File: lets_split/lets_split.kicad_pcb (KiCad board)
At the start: 2 copper layers, 112 x 79 mm, 62 parts, among them J1 3PIN, J2 6PIN, J3 3PIN, SW1 SW_PUSH, SW10 SW_PUSH, SW11 SW_PUSH, SW12 SW_PUSH, SW13 SW_PUSH, SW14 SW_PUSH, SW15 SW_PUSH, SW16 SW_PUSH, SW17 SW_PUSH, SW18 SW_PUSH, SW19 SW_PUSH, SW2 SW_PUSH, SW21 SW_PUSH, SW22 SW_PUSH, SW23 SW_PUSH, SW3 SW_PUSH, SW4 SW_PUSH, SW5 SW_PUSH, SW6 SW_PUSH, SW7 SW_PUSH, SW8 SW_PUSH, SW9 SW_PUSH, U2 HOLE, U3 HOLE, U4 HOLE, U5 HOLE

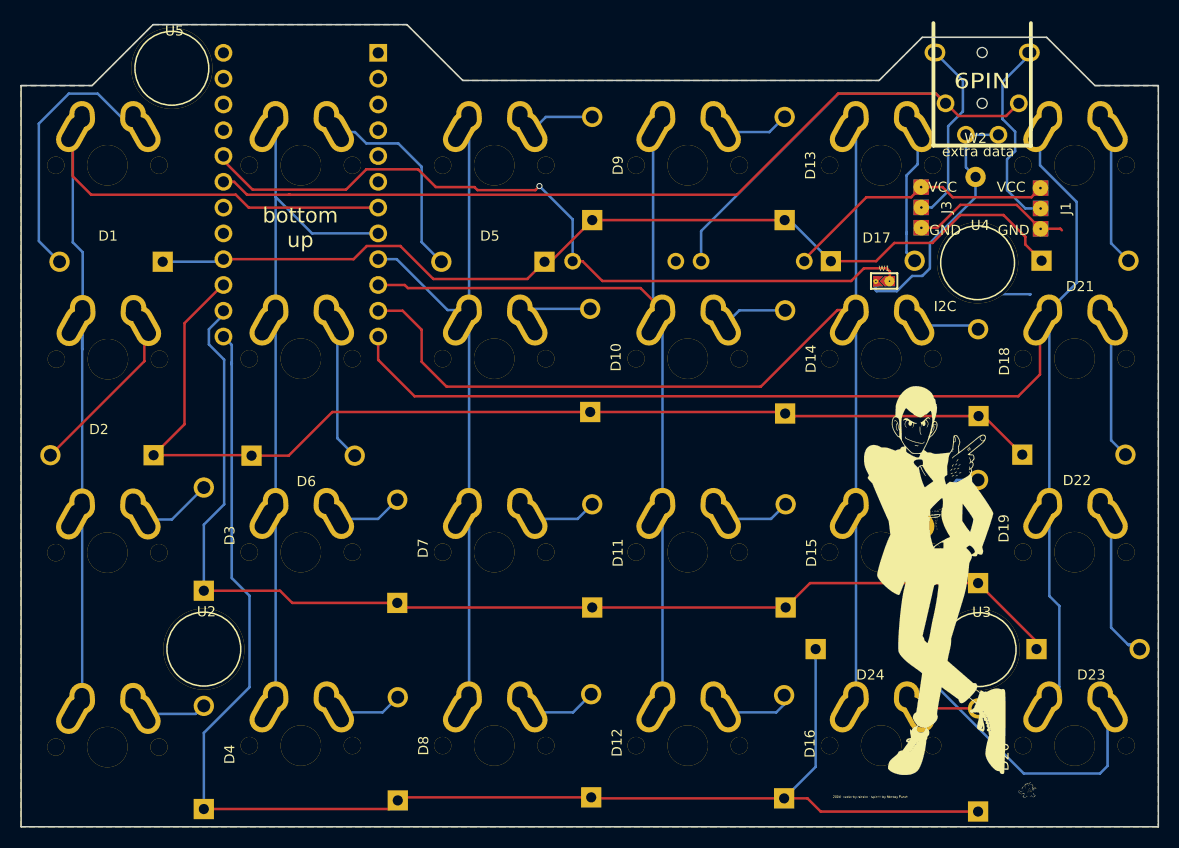
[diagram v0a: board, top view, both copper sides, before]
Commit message: Fix column 1 spacing
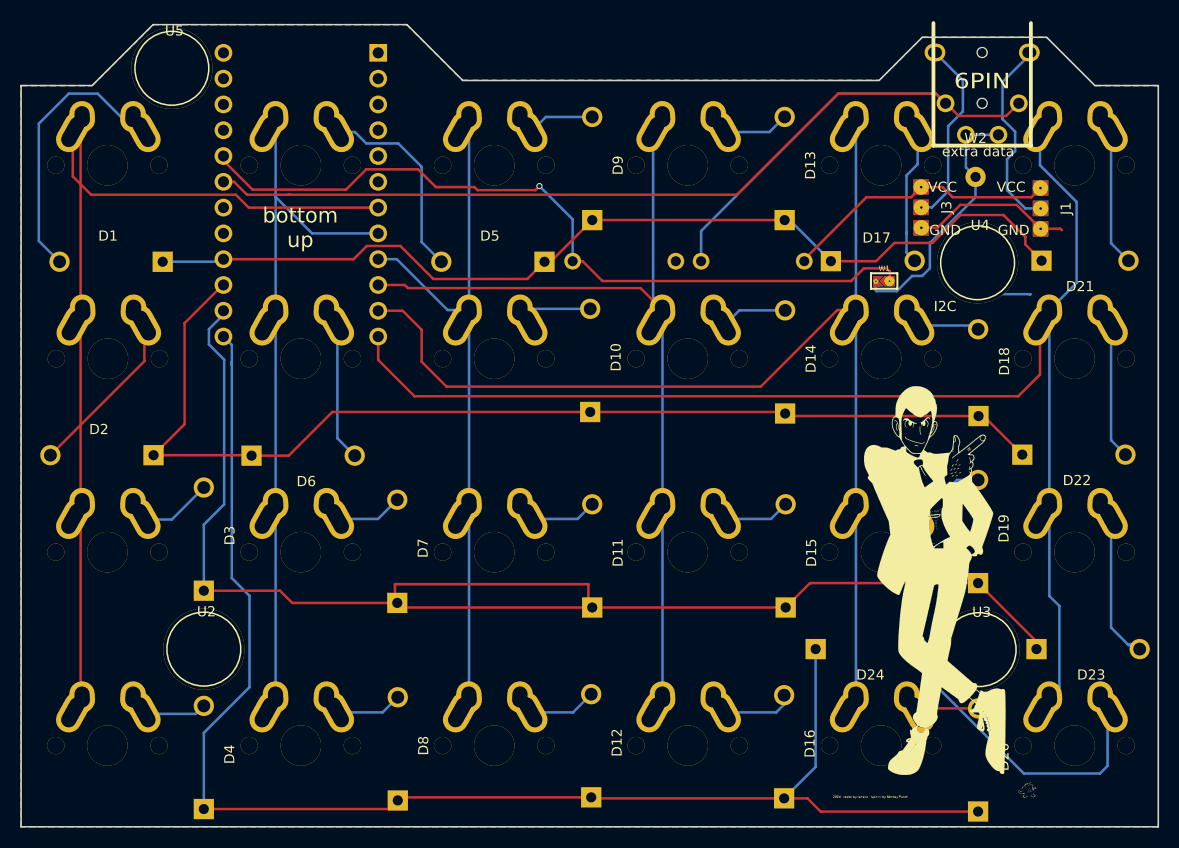
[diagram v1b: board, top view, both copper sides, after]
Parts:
- moved SW4 0.15 mm to (45.5, 104.0)
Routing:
- net row2: track 117.3 -> 142.1 mm
- net col0: track 96.5 -> 98.4 mm
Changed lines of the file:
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@@
-(kicad_pcb (version 4) (host pcbnew 4.0.2-stable)
+(kicad_pcb (version 4) (host pcbnew 4.0.7)
   (general
     (links 160)
-    (no_connects 2)
-    (area 36.386172 31.485 149.075001 114.5692)
+    (no_connects 0)
+    (area 35.71875 30.95625 150.01875 114.3)
     (thickness 1.6)
     (drawings 29)
-    (tracks 287)
+    (tracks 291)
     (zones 0)
     (modules 62)
@@
     (add_net xtradata)
   )
+  (module flipalps:MXALPS_FLIP (layer F.Cu)
+    (at 45.55 65.9)
+    (descr MXALPS)
+    (tags MXALPS)
+    (fp_text reference SW2 (at 0 3.048) (layer B.SilkS) hide
+      (effects (font (thickness 0.3048)) (justify mirror))
+    )
+    (fp_text value SW_PUSH (at -3.5 9) (layer B.SilkS) hide
+      (effects (font (thickness 0.3048)) (justify mirror))
+    )
+    (fp_line (start -7.75 6.4) (end -7.75 -6.4) (layer Dwgs.User) (width 0.3))
+    (fp_line (start -7.75 6.4) (end 7.75 6.4) (layer Dwgs.User) (width 0.3))
+    (fp_line (start 7.75 6.4) (end 7.75 -6.4) (layer Dwgs.User) (width 0.3))
+    (fp_line (start 7.75 -6.4) (end -7.75 -6.4) (layer Dwgs.User) (width 0.3))
+    (fp_line (start -7.62 -7.62) (end 7.62 -7.62) (layer Dwgs.User) (width 0.3))
+    (fp_line (start 7.62 -7.62) (end 7.62 7.62) (layer Dwgs.User) (width 0.3))
+    (fp_line (start 7.62 7.62) (end -7.62 7.62) (layer Dwgs.User) (width 0.3))
+    (fp_line (start -7.62 7.62) (end -7.62 -7.62) (layer Dwgs.User) (width 0.3))
+    (pad 1 thru_hole oval (at -2.48 -4.79 3.9) (size 2.5 3.08) (drill oval 1.5 2.08) (layers *.Cu *.Mask F.SilkS)
+      (net 36 col0))
+    (pad 2 thru_hole oval (at 3.595 -3.27 29) (size 2.5 4.17) (drill oval 1.5 3.17) (layers *.Cu *.Mask F.SilkS)
+      (net 3 "Net-(D2-Pad2)"))
+    (pad "" np_thru_hole circle (at 0 0) (size 3.98781 3.98781) (drill 3.9878) (layers *.Cu *.Mask F.SilkS)
+      (clearance 0.1524))
+    (pad "" np_thru_hole circle (at -5.08 0) (size 1.70181 1.70181) (drill 1.7018) (layers *.Cu *.Mask F.SilkS)
+      (clearance 0.1524))
+    (pad "" np_thru_hole circle (at 5.08 0) (size 1.70181 1.70181) (drill 1.7018) (layers *.Cu *.Mask F.SilkS)
+      (clearance 0.1524))
+    (pad 1 thru_hole oval (at -3.405 -3.27 330.95) (size 2.5 4.17) (drill oval 1.5 3.17) (layers *.Cu *.Mask F.SilkS)
+      (net 36 col0))
+    (pad 2 thru_hole oval (at 2.52 -4.79 356.1) (size 2.5 3.08) (drill oval 1.5 2.08) (layers *.Cu *.Mask F.SilkS)
+      (net 3 "Net-(D2-Pad2)"))
+  )
   (module Diodes_ThroughHole:Diode_DO-41_SOD81_Horizontal_RM10 (layer F.Cu)
     (at 131.25 110.5 90)
@@
   )
   (module flipalps:MXALPS_FLIP (layer F.Cu)
-    (at 45.55 65.95)
-    (descr MXALPS)
-    (tags MXALPS)
-    (fp_text reference SW2 (at 0 3.048) (layer B.SilkS) hide
-      (effects (font (thickness 0.3048)) (justify mirror))
-    )
-    (fp_text value SW_PUSH (at -3.5 9) (layer B.SilkS) hide
-      (effects (font (thickness 0.3048)) (justify mirror))
-    )
-    (fp_line (start -7.75 6.4) (end -7.75 -6.4) (layer Dwgs.User) (width 0.3))
-    (fp_line (start -7.75 6.4) (end 7.75 6.4) (layer Dwgs.User) (width 0.3))
-    (fp_line (start 7.75 6.4) (end 7.75 -6.4) (layer Dwgs.User) (width 0.3))
-    (fp_line (start 7.75 -6.4) (end -7.75 -6.4) (layer Dwgs.User) (width 0.3))
-    (fp_line (start -7.62 -7.62) (end 7.62 -7.62) (layer Dwgs.User) (width 0.3))
-    (fp_line (start 7.62 -7.62) (end 7.62 7.62) (layer Dwgs.User) (width 0.3))
-    (fp_line (start 7.62 7.62) (end -7.62 7.62) (layer Dwgs.User) (width 0.3))
-    (fp_line (start -7.62 7.62) (end -7.62 -7.62) (layer Dwgs.User) (width 0.3))
-    (pad 1 thru_hole oval (at -2.48 -4.79 3.9) (size 2.5 3.08) (drill oval 1.5 2.08) (layers *.Cu *.Mask F.SilkS)
-      (net 36 col0))
-    (pad 2 thru_hole oval (at 3.595 -3.27 29) (size 2.5 4.17) (drill oval 1.5 3.17) (layers *.Cu *.Mask F.SilkS)
-      (net 3 "Net-(D2-Pad2)"))
-    (pad "" np_thru_hole circle (at 0 0) (size 3.98781 3.98781) (drill 3.9878) (layers *.Cu *.Mask F.SilkS)
-      (clearance 0.1524))
-    (pad "" np_thru_hole circle (at -5.08 0) (size 1.70181 1.70181) (drill 1.7018) (layers *.Cu *.Mask F.SilkS)
-      (clearance 0.1524))
-    (pad "" np_thru_hole circle (at 5.08 0) (size 1.70181 1.70181) (drill 1.7018) (layers *.Cu *.Mask F.SilkS)
-      (clearance 0.1524))
-    (pad 1 thru_hole oval (at -3.405 -3.27 330.95) (size 2.5 4.17) (drill oval 1.5 3.17) (layers *.Cu *.Mask F.SilkS)
-      (net 36 col0))
-    (pad 2 thru_hole oval (at 2.52 -4.79 356.1) (size 2.5 3.08) (drill oval 1.5 2.08) (layers *.Cu *.Mask F.SilkS)
-      (net 3 "Net-(D2-Pad2)"))
-  )
-  (module flipalps:MXALPS_FLIP (layer F.Cu)
-    (at 45.5 85)
+    (at 45.5 84.95)
     (descr MXALPS)
     (tags MXALPS)
@@
   )
   (module flipalps:MXALPS_FLIP (layer F.Cu)
-    (at 45.5 104.15)
+    (at 45.5 104)
     (descr MXALPS)
     (tags MXALPS)
@@
   (segment (start 49.095 81.73) (end 51.85746 81.73) (width 0.25) (layer B.Cu) (net 5))
   (segment (start 51.85746 81.73) (end 54.99746 78.59) (width 0.25) (layer B.Cu) (net 5))
+  (segment (start 74.04746 89.95) (end 73.81875 90.4875) (width 0.25) (layer F.Cu) (net 6) (status 80000))
+  (segment (start 73.81875 90.4875) (end 73.81875 88.10625) (width 0.25) (layer F.Cu) (net 6) (status 80000))
+  (segment (start 73.81875 88.10625) (end 92.86875 88.10625) (width 0.25) (layer F.Cu) (net 6) (status 80000))
+  (segment (start 92.86875 88.10625) (end 92.86875 90.4875) (width 0.25) (layer F.Cu) (net 6) (status 80000))
+  (segment (start 92.86875 90.4875) (end 93.24746 90.4) (width 0.25) (layer F.Cu) (net 6) (status 80000))
   (segment (start 131.24746 88) (end 114.69746 88) (width 0.25) (layer F.Cu) (net 6))
   (segment (start 114.69746 88) (end 112.29746 90.4) (width 0.25) (layer F.Cu) (net 6))
@@
   (segment (start 112.29746 90.4) (end 74.49746 90.4) (width 0.25) (layer F.Cu) (net 6))
   (segment (start 74.49746 90.4) (end 73.99746 89.9) (width 0.25) (layer F.Cu) (net 6))
-  (segment (start 49.095 100.88) (end 54.20746 100.88) (width 0.25) (layer B.Cu) (net 7))
+  (segment (start 49.095 100.88) (end 54.20746 100.88) (width 0.25) (layer B.Cu) (net 7) (status 10))
   (segment (start 54.20746 100.88) (end 54.99746 100.09) (width 0.25) (layer B.Cu) (net 7))
-  (segment (start 48.64 98.74) (end 48.02 99.36) (width 0.25) (layer B.Cu) (net 7))
-  (segment (start 48.02 99.36) (end 49.095 100.88) (width 0.25) (layer B.Cu) (net 7))
+  (segment (start 48.64 98.74) (end 48.02 99.36) (width 0.25) (layer B.Cu) (net 7) (status 30))
+  (segment (start 48.02 99.36) (end 49.095 100.88) (width 0.25) (layer B.Cu) (net 7) (status 30))
   (segment (start 131.24746 110.5) (end 115.75 110.5) (width 0.25) (layer F.Cu) (net 8))
   (segment (start 114.45 109.2) (end 112.14746 109.2) (width 0.25) (layer F.Cu) (net 8))
@@
   (segment (start 88.05 48.9) (end 91.32 52.17) (width 0.25) (layer B.Cu) (net 35))
   (segment (start 91.32 52.17) (end 91.32 56.3) (width 0.25) (layer B.Cu) (net 35))
-  (segment (start 43.02 65) (end 43.02 63.555) (width 0.25) (layer B.Cu) (net 36))
-  (segment (start 43.02 63.555) (end 42.145 62.68) (width 0.25) (layer B.Cu) (net 36))
-  (segment (start 42.145 62.68) (end 42.145 62.085) (width 0.25) (layer B.Cu) (net 36))
-  (segment (start 42.145 62.085) (end 43.07 61.16) (width 0.25) (layer B.Cu) (net 36))
+  (segment (start 42.145 62.63) (end 42.8625 61.9125) (width 0.25) (layer F.Cu) (net 36) (status 80000))
+  (segment (start 42.8625 61.9125) (end 42.8625 80.9625) (width 0.25) (layer F.Cu) (net 36) (status 80000))
+  (segment (start 42.8625 80.9625) (end 43.02 80.16) (width 0.25) (layer F.Cu) (net 36) (status 80000))
+  (segment (start 42.095 43.58) (end 42.8625 42.8625) (width 0.25) (layer F.Cu) (net 36) (status 80000))
+  (segment (start 42.8625 42.8625) (end 42.8625 61.9125) (width 0.25) (layer F.Cu) (net 36) (status 80000))
+  (segment (start 42.8625 61.9125) (end 43.07 61.11) (width 0.25) (layer F.Cu) (net 36) (status 80000))
+  (segment (start 42.095 81.68) (end 42.8625 80.9625) (width 0.25) (layer F.Cu) (net 36) (status 80000))
+  (segment (start 42.8625 80.9625) (end 42.8625 100.0125) (width 0.25) (layer F.Cu) (net 36) (status 80000))
+  (segment (start 42.8625 100.0125) (end 43.02 99.21) (width 0.25) (layer F.Cu) (net 36) (status 80000))
   (segment (start 72.17 51.02) (end 59.42 51.02) (width 0.25) (layer F.Cu) (net 36))
   (segment (start 42.095 47.945) (end 42.095 43.58) (width 0.25) (layer F.Cu) (net 36))
@@
   (segment (start 58.15 49.75) (end 43.9 49.75) (width 0.25) (layer F.Cu) (net 36))
   (segment (start 59.42 51.02) (end 58.15 49.75) (width 0.25) (layer F.Cu) (net 36))
-  (segment (start 42.095 43.58) (end 42.095 54.445) (width 0.25) (layer B.Cu) (net 36))
-  (segment (start 43.07 55.42) (end 43.07 61.755) (width 0.25) (layer B.Cu) (net 36))
-  (segment (start 42.095 54.445) (end 43.07 55.42) (width 0.25) (layer B.Cu) (net 36))
-  (segment (start 43.07 61.755) (end 43.02 61.805) (width 0.25) (layer B.Cu) (net 36))
-  (segment (start 43.02 61.805) (end 43.02 65) (width 0.25) (layer B.Cu) (net 36))
-  (segment (start 43.02 65) (end 43.02 99.36) (width 0.25) (layer B.Cu) (net 36))
   (segment (start 72.17 53.56) (end 65.66 53.56) (width 0.25) (layer B.Cu) (net 37))
   (segment (start 65.66 53.56) (end 62.07 49.97) (width 0.25) (layer B.Cu) (net 37))
